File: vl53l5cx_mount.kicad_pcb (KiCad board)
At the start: 2 copper layers, 12.7 x 7.9 mm, 10 parts, among them J1 Conn_01x05_MountingPin, U1 VL53L5CXV0GC/1

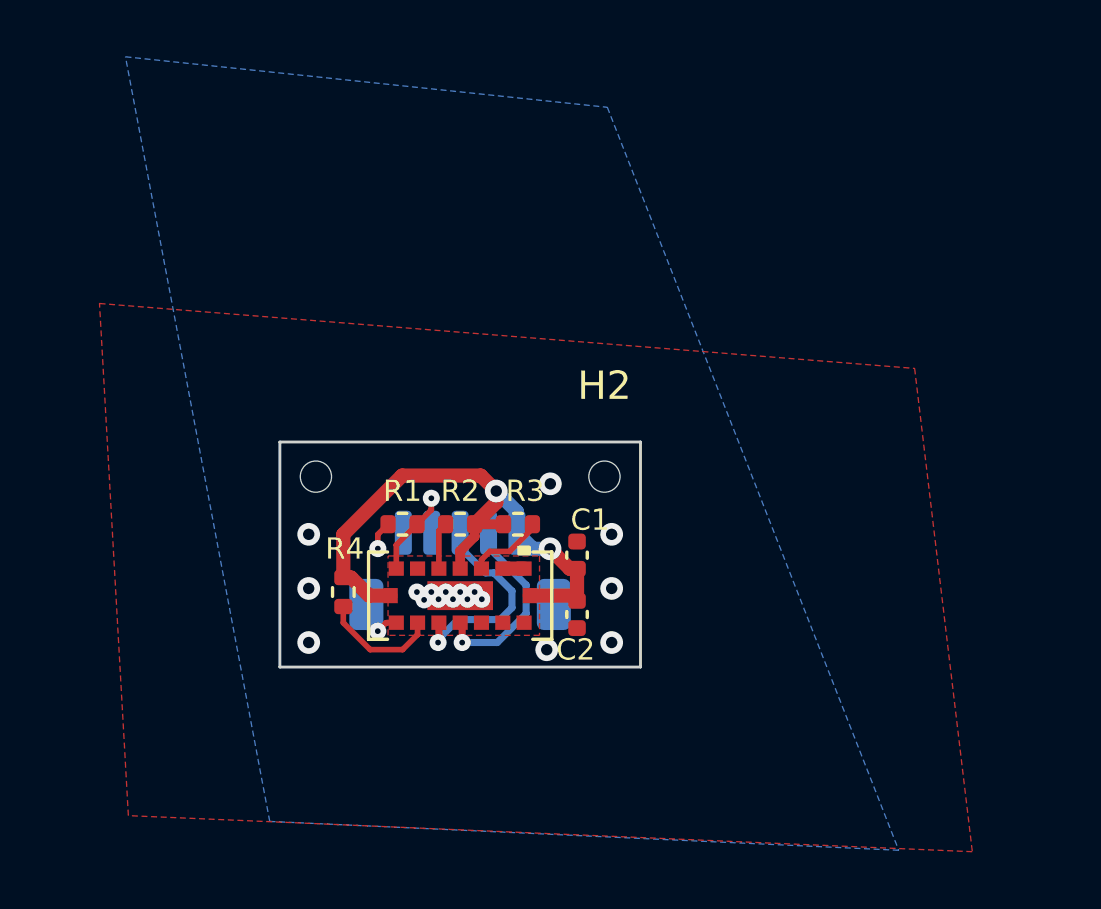
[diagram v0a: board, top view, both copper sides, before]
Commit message: reduced component count
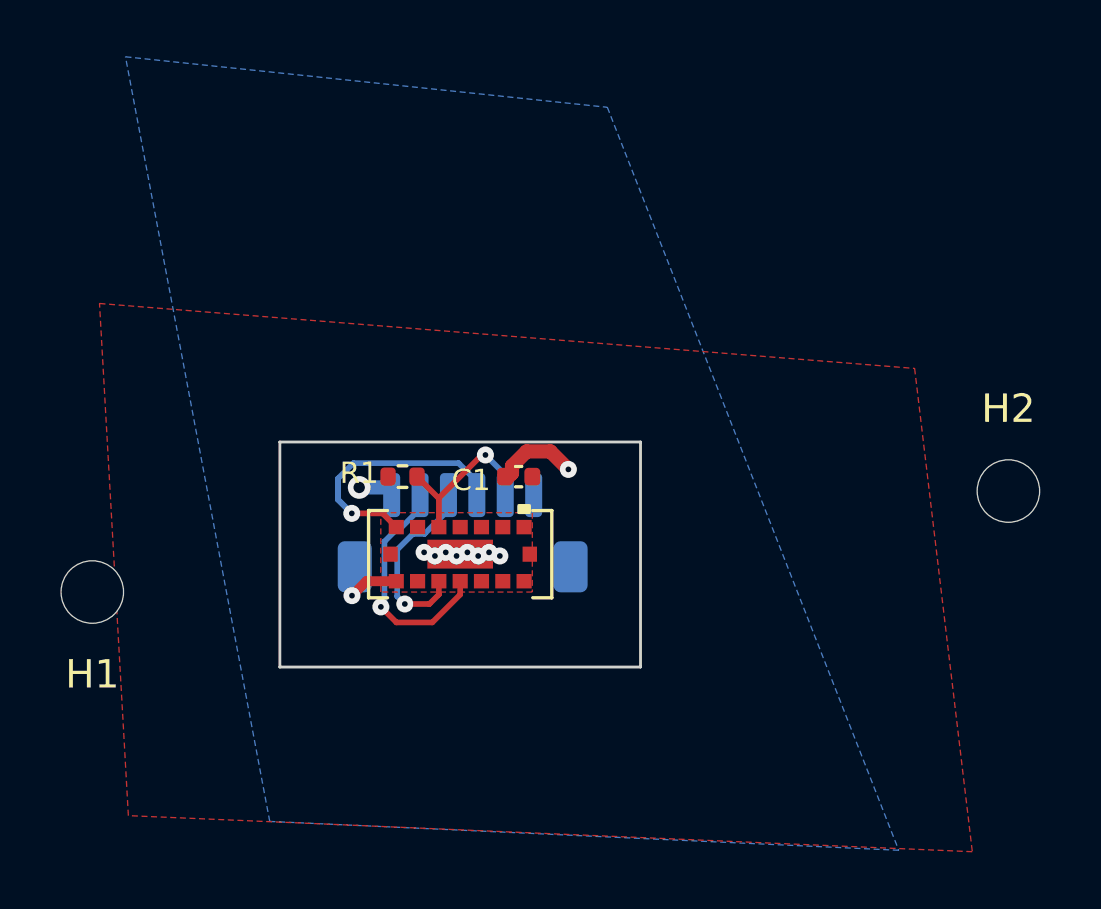
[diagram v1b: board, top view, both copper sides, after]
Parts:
- removed C2: 0.1u, Capacitor_SMD:C_0402_1005Metric
- removed R2, R3, R4: 47k, Resistor_SMD:R_0402_1005Metric
- H1, H2: footprint scew:m1 -> MountingHole:MountingHole_2.2mm_M2_DIN965
- J1: value Conn_01x05_MountingPin -> Conn_01x06_MountingPin; footprint Connector_JST:JST_SH_BM05B-SRSS-TB_1x05-1MP_P1.00mm_Vertical -> Connector_JST:JST_SH_BM06B-SRSS-TB_1x06-1MP_P1.00mm_Vertical
- moved H2 14.2 mm to (143.8, 26.2)
- moved H1 8.86 mm to (111.5, 29.7)
- moved C1 3.45 mm to (126.5, 25.7), turned to 180 degrees
- moved R1 1.68 mm to (122.4, 25.7)
- moved U1 1.46 mm to (124.5, 28.4)
- moved J1 1.33 mm to (124.5, 27.6)
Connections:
- J1 pad 1: Earth -> VCC
- J1 pad 2: /RST -> /SCL
- J1 pad 4: /SCL -> /RST
- J1 pad 5: VCC -> /INT
- R1 pad 1: /RST -> /INT
- R1 pad 2: Earth -> VCC
- U1 pad A3: Net-(R2-Pad1) -> /INT
- U1 pad A5: Net-(R3-Pad1) -> VCC
- U1 pad C2: Net-(R4-Pad1) -> unconnected-(U1-PadC2)
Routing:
- net VCC: track 21.3 -> 1.14 mm, vias 2 -> 1
- net /RST: track 4.11 -> 10.5 mm
- net /INT: track 0.00 -> 6.08 mm, vias 0 -> 1
- net Net-(R4-Pad1): track 4.22 -> 0.00 mm
- net Net-(R3-Pad1): track 2.78 -> 0.00 mm
- net Earth: track 2.52 -> 4.65 mm, vias 20 -> 10
- net /SCL: track 6.80 -> 8.46 mm
- net Net-(R2-Pad1): track 1.66 -> 0.00 mm
- net /SDA: track 7.45 -> 6.74 mm
- added copper zone on F.Cu, net VCC

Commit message: clean up DRC
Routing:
- net VCC: track 1.14 -> 26.7 mm
- net Earth: track 4.65 -> 4.71 mm, vias 10 -> 7
- removed copper zone on F.Cu, net VCC
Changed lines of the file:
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@@
     (property "Sheetname" "")
     (attr smd)
-    (fp_text reference "C1" (at 1.679 -0.127 180) (layer "F.SilkS")
+    (fp_text reference "C1" (at 1.679 0.127 180) (layer "F.SilkS")
       (effects (font (size 0.75 0.75) (thickness 0.1)))
     )
@@
     (property "Sheetname" "")
     (attr smd)
-    (fp_text reference "R1" (at 1.526 0.127) (layer "F.SilkS")
+    (fp_text reference "R1" (at 1.526 0.254) (layer "F.SilkS")
       (effects (font (size 0.75 0.75) (thickness 0.1)))
     )
@@
   (gr_line (start 118.11 32.3596) (end 118.11 24.4348) (layer "Edge.Cuts") (width 0.1))
   (gr_line (start 118.11 24.4348) (end 130.81 24.4348) (layer "Edge.Cuts") (width 0.1))
+  (segment (start 120.949001 28.3845) (end 119.850489 29.483012) (width 0.5) (layer "F.Cu") (net 1))
+  (segment (start 121.062776 31.388456) (end 125.932756 31.388456) (width 0.5) (layer "F.Cu") (net 1))
+  (segment (start 125.210001 26.812277) (end 125.606278 26.416) (width 0.35) (layer "F.Cu") (net 1))
+  (segment (start 126.386351 26.416) (end 127 25.802351) (width 0.35) (layer "F.Cu") (net 1))
+  (segment (start 125.210001 27.432) (end 124.46 27.432) (width 0.35) (layer "F.Cu") (net 1))
+  (segment (start 120.425441 26.035) (end 120.904 26.035) (width 0.5) (layer "F.Cu") (net 1))
+  (segment (start 119.850489 30.176169) (end 121.062776 31.388456) (width 0.5) (layer "F.Cu") (net 1))
+  (segment (start 120.949001 28.3845) (end 119.84364 27.279139) (width 0.5) (layer "F.Cu") (net 1))
+  (segment (start 127.476212 28.670212) (end 127.1905 28.3845) (width 0.5) (layer "F.Cu") (net 1))
+  (segment (start 127 25.654) (end 127.476212 26.130212) (width 0.5) (layer "F.Cu") (net 1))
+  (segment (start 125.606278 26.416) (end 126.386351 26.416) (width 0.35) (layer "F.Cu") (net 1))
+  (segment (start 119.84364 26.616801) (end 120.425441 26.035) (width 0.5) (layer "F.Cu") (net 1))
+  (segment (start 122.0089 28.3845) (end 120.949001 28.3845) (width 0.5) (layer "F.Cu") (net 1))
+  (segment (start 127.476212 26.130212) (end 127.476212 28.670212) (width 0.5) (layer "F.Cu") (net 1))
+  (segment (start 119.850489 29.483012) (end 119.850489 30.176169) (width 0.5) (layer "F.Cu") (net 1))
+  (segment (start 125.210001 27.432) (end 125.210001 26.812277) (width 0.35) (layer "F.Cu") (net 1))
+  (segment (start 121.285 25.654) (end 120.904 26.035) (width 0.2) (layer "F.Cu") (net 1))
+  (segment (start 127 25.802351) (end 127 25.654) (width 0.35) (layer "F.Cu") (net 1))
+  (segment (start 121.92 25.654) (end 121.285 25.654) (width 0.2) (layer "F.Cu") (net 1))
+  (segment (start 119.84364 27.279139) (end 119.84364 26.616801) (width 0.5) (layer "F.Cu") (net 1))
+  (segment (start 127.1905 28.3845) (end 126.9111 28.3845) (width 0.5) (layer "F.Cu") (net 1))
+  (segment (start 125.932756 31.388456) (end 127.476212 29.845) (width 0.5) (layer "F.Cu") (net 1))
+  (segment (start 127.476212 29.845) (end 127.476212 28.670212) (width 0.5) (layer "F.Cu") (net 1))
   (via (at 120.904 26.035) (size 0.8) (drill 0.4) (layers "F.Cu" "B.Cu") (net 1))
   (segment (start 122.047 26.035) (end 120.904 26.035) (width 0.5) (layer "B.Cu") (net 1))
-  (segment (start 126.283972 25.282611) (end 126.801583 24.765) (width 0.5) (layer "F.Cu") (net 2))
-  (segment (start 127.635 24.765) (end 128.27 25.4) (width 0.5) (layer "F.Cu") (net 2))
   (segment (start 122.209999 29.337) (end 121.158 29.337) (width 0.35) (layer "F.Cu") (net 2))
-  (segment (start 126.283972 25.537028) (end 126.283972 25.282611) (width 0.5) (layer "F.Cu") (net 2))
-  (segment (start 126.801583 24.765) (end 127.635 24.765) (width 0.5) (layer "F.Cu") (net 2))
+  (segment (start 126.04 25.654) (end 126.04 25.399583) (width 0.5) (layer "F.Cu") (net 2))
+  (segment (start 126.595103 24.84448) (end 127.71448 24.84448) (width 0.5) (layer "F.Cu") (net 2))
+  (segment (start 126.04 25.399583) (end 126.595103 24.84448) (width 0.5) (layer "F.Cu") (net 2))
   (segment (start 121.158 29.337) (end 120.65 29.845) (width 0.35) (layer "F.Cu") (net 2))
-  (segment (start 126.167 25.654) (end 126.283972 25.537028) (width 0.5) (layer "F.Cu") (net 2))
-  (via (at 125.476 28.321) (size 0.6) (drill 0.2) (layers "F.Cu" "B.Cu") (net 2))
-  (via (at 125.857 28.448) (size 0.6) (drill 0.2) (layers "F.Cu" "B.Cu") (free) (net 2))
-  (via (at 123.19 28.321) (size 0.6) (drill 0.2) (layers "F.Cu" "B.Cu") (free) (net 2))
+  (segment (start 127.71448 24.84448) (end 128.27 25.4) (width 0.5) (layer "F.Cu") (net 2))
+  (via (at 125.857 28.321) (size 0.6) (drill 0.2) (layers "F.Cu" "B.Cu") (free) (net 2))
+  (via (at 125.222 28.321) (size 0.6) (drill 0.2) (layers "F.Cu" "B.Cu") (net 2))
+  (via (at 123.317 28.321) (size 0.6) (drill 0.2) (layers "F.Cu" "B.Cu") (free) (net 2))
   (via (at 120.65 29.845) (size 0.6) (drill 0.2) (layers "F.Cu" "B.Cu") (net 2))
-  (via (at 124.714 28.321) (size 0.6) (drill 0.2) (layers "F.Cu" "B.Cu") (net 2))
+  (via (at 124.587 28.321) (size 0.6) (drill 0.2) (layers "F.Cu" "B.Cu") (net 2))
   (via (at 123.952 28.321) (size 0.6) (drill 0.2) (layers "F.Cu" "B.Cu") (net 2))
-  (via (at 125.095 28.448) (size 0.6) (drill 0.2) (layers "F.Cu" "B.Cu") (net 2))
   (via (at 128.27 25.4) (size 0.6) (drill 0.2) (layers "F.Cu" "B.Cu") (net 2))
-  (via (at 123.571 28.448) (size 0.6) (drill 0.2) (layers "F.Cu" "B.Cu") (net 2))
-  (via (at 124.333 28.448) (size 0.6) (drill 0.2) (layers "F.Cu" "B.Cu") (net 2))
   (segment (start 122.21551 30.788936) (end 123.477785 30.788936) (width 0.2) (layer "F.Cu") (net 3))
   (segment (start 121.667683 30.241109) (end 122.21551 30.788936) (width 0.2) (layer "F.Cu") (net 3))
@@
   (segment (start 126.047 26.304) (end 126.047 25.59) (width 0.2) (layer "B.Cu") (net 7))
   (segment (start 126.047 25.59) (end 125.349 24.892) (width 0.2) (layer "B.Cu") (net 7))
-  (zone (net 1) (net_name "VCC") (layer "F.Cu") (hatch edge 0.508)
-    (connect_pads (clearance 0.3))
-    (min_thickness 0.254) (filled_areas_thickness no)
-    (fill yes (thermal_gap 0.508) (thermal_bridge_width 0.3))
-    (polygon
-      (pts
-        (xy 140.462 21.844)
-        (xy 142.494 38.862)
-        (xy 112.776 37.592)
-        (xy 111.76 19.558)
-      )
-    )
-  )
   (zone (net 2) (net_name "Earth") (layer "F.Cu") (hatch edge 0.508)
     (connect_pads yes (clearance 0.3))
@@
     (polygon
       (pts
-        (xy 127 29.718)
-        (xy 121.666 29.718)
-        (xy 121.666 26.924)
-        (xy 127 26.924)
+        (xy 127 29.591)
+        (xy 121.666 29.591)
+        (xy 121.666 27.178)
+        (xy 127 27.178)
       )
     )

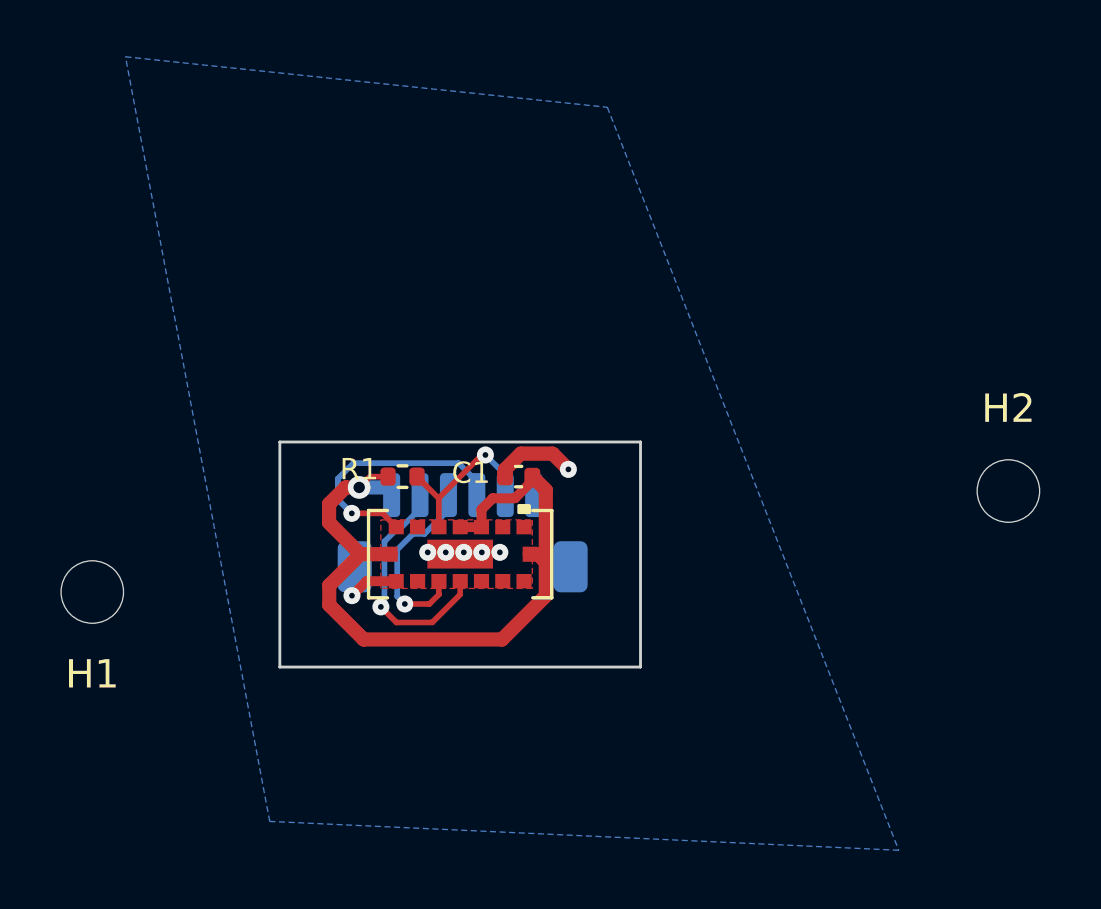
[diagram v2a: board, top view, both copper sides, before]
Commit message: fix connector and edges
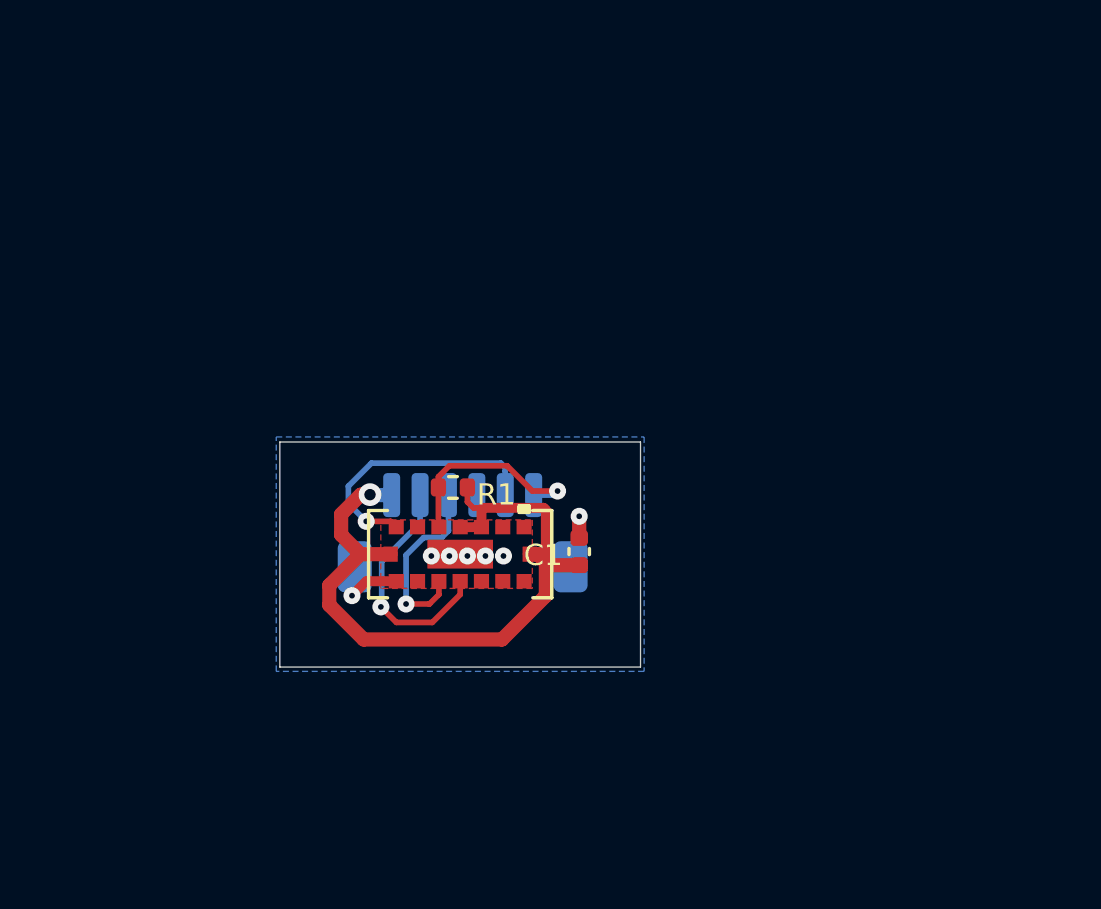
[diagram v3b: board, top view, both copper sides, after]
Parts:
- removed H1, H2: MountingHole, MountingHole:MountingHole_2.2mm_M2_DIN965
- moved C1 3.39 mm to (128.7, 28.3), turned to 90 degrees
- moved R1 1.81 mm to (124.2, 26.0), turned to 0 degrees
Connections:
- J1 pad 4: /RST -> Earth
- J1 pad 5: /INT -> /RST
- J1 pad 6: Earth -> /INT
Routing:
- net Earth: track 4.71 -> 2.53 mm
- net /INT: track 6.08 -> 7.40 mm
- net /RST: track 10.5 -> 9.53 mm
- net VCC: track 26.7 -> 26.0 mm

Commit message: update silkscreen
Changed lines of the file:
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@@
     (property "Sheetname" "")
     (attr smd)
-    (fp_text reference "C1" (at -0.127 -1.27) (layer "F.SilkS")
+    (fp_text reference "C1" (at -1.552 0) (layer "F.SilkS")
       (effects (font (size 0.75 0.75) (thickness 0.1)))
     )
@@
     (property "Sheetname" "")
     (attr smd)
-    (fp_text reference "R1" (at 1.526 0.254) (layer "F.SilkS")
+    (fp_text reference "R1" (at 1.653 0) (layer "F.SilkS")
       (effects (font (size 0.75 0.75) (thickness 0.1)))
     )
